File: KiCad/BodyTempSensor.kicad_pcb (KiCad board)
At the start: 2 copper layers, 62 parts, among them IC1 MAX30208CLB+T, J1 USB_C_Receptacle_USB2.0, J2 BAT, J3 TC2030, U1 nRF52840, U2 USBLC6-2SC6, U3 MCP73833-xxx-UN, U4 TLV62568DBVR, U5 MCP6001-OT, Y1 32MHz

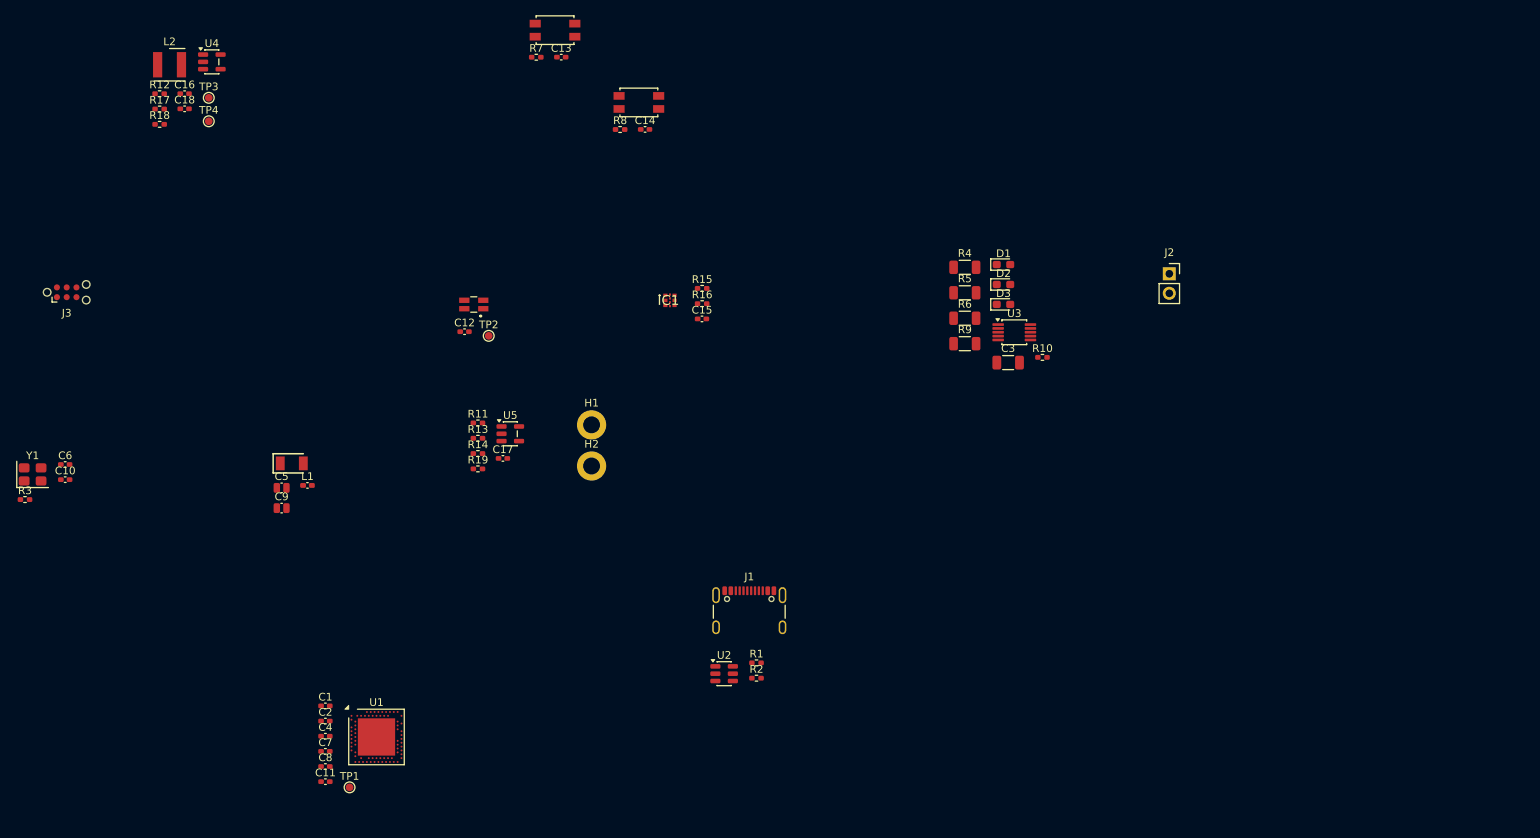
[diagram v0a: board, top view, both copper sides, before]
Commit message: Changed temp sensor, added components and created a general layout design
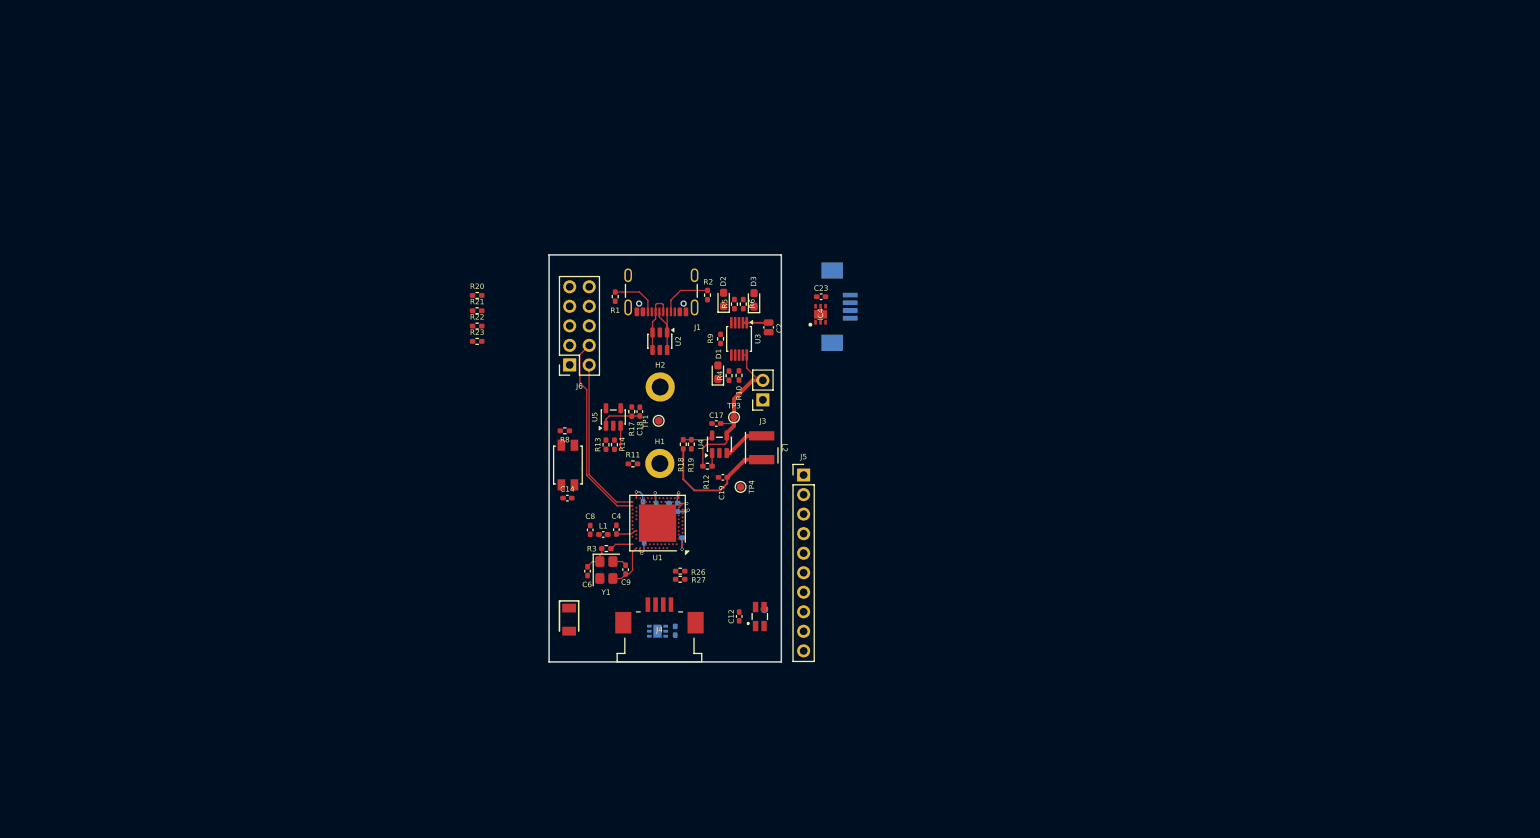
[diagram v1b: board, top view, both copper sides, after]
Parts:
- removed C13, C15: 100n, Capacitor_SMD:C_0402_1005Metric_Pad0.74x0.62mm_HandSolder
- removed C16: 4u7, Capacitor_SMD:C_0402_1005Metric_Pad0.74x0.62mm_HandSolder
- removed IC1: MAX30208CLB+T, PCB_Lib_ItsNotDaan:MAX30208CLBT
- removed J2: BAT, Connector_PinSocket_2.54mm:PinSocket_1x02_P2.54mm_Vertical
- removed R15, R16: 5k1, Resistor_SMD:R_0402_1005Metric_Pad0.72x0.64mm_HandSolder
- removed R7: 10k, Resistor_SMD:R_0402_1005Metric_Pad0.72x0.64mm_HandSolder
- removed RST1: SW_RST, PCB_Lib_ItsNotDaan:SW_SPST_EVQP2
- added C19: 10u, Capacitor_SMD:C_0402_1005Metric_Pad0.74x0.62mm_HandSolder, F.Cu at (120.8, 86.6)
- added C22: 100n, Capacitor_SMD:C_0402_1005Metric_Pad0.74x0.62mm_HandSolder, B.Cu at (114.7, 106.5)
- added C23: 100n, Capacitor_SMD:C_0402_1005Metric_Pad0.74x0.62mm_HandSolder, F.Cu at (133.6, 63.1)
- added IC3: TMP117MAIDRVT, LibLoader:SON65P200X200X80-7N, B.Cu at (112.3, 106.6)
- added IC4: TMP117MAIDRVT, LibLoader:SON65P200X200X80-7N, F.Cu at (133.6, 65.4)
- added J4: 52271-0479, LibLoader:522710479, F.Cu at (112.6, 106.9)
- added J5: Conn_01x10, Connector_PinHeader_2.54mm:PinHeader_1x10_P2.54mm_Vertical, F.Cu at (131.3, 86.3)
- added J6: Conn_02x05_Odd_Even, Connector_PinSocket_2.54mm:PinSocket_2x05_P2.54mm_Vertical, F.Cu at (100.9, 72.0)
- added J7: 52271-0479, LibLoader:522710479, B.Cu at (133.7, 64.4)
- added R20: 10k, Resistor_SMD:R_0402_1005Metric_Pad0.72x0.64mm_HandSolder, F.Cu at (88.9, 63.0)
- added R21: 180k, Resistor_SMD:R_0402_1005Metric_Pad0.72x0.64mm_HandSolder, F.Cu at (88.9, 64.9)
- added R22: 47k, Resistor_SMD:R_0402_1005Metric_Pad0.72x0.64mm_HandSolder, F.Cu at (88.9, 66.9)
- added R23: 180k, Resistor_SMD:R_0402_1005Metric_Pad0.72x0.64mm_HandSolder, F.Cu at (88.9, 68.9)
- added R26: 5k1, Resistor_SMD:R_0402_1005Metric_Pad0.72x0.64mm_HandSolder, F.Cu at (115.3, 98.8)
- added R27: 5k1, Resistor_SMD:R_0402_1005Metric_Pad0.72x0.64mm_HandSolder, F.Cu at (115.3, 99.8)
- C1, C11, C7, TP2: moved to B.Cu
- C10: value 12p -> 100n; moved to B.Cu
- C17: value 270n -> 4u7
- C18: value 10u -> 270n
- C2: value 100n -> 1u; footprint Capacitor_SMD:C_0402_1005Metric_Pad0.74x0.62mm_HandSolder -> Capacitor_SMD:C_0504_1310Metric_Pad0.83x1.28mm_HandSolder
- C3: value 1u -> 100n; footprint Capacitor_SMD:C_1206_3216Metric -> Capacitor_SMD:C_0402_1005Metric_Pad0.74x0.62mm_HandSolder; moved to B.Cu
- C4: value 100n -> 0p8
- C5: value 0p8 -> 100n; footprint Capacitor_SMD:C_0504_1310Metric_Pad0.83x1.28mm_HandSolder -> Capacitor_SMD:C_0402_1005Metric_Pad0.74x0.62mm_HandSolder; moved to B.Cu
- C8: value 100n -> 0p5
- C9: value 0p5 -> 12p; footprint Capacitor_SMD:C_0504_1310Metric_Pad0.83x1.28mm_HandSolder -> Capacitor_SMD:C_0402_1005Metric_Pad0.74x0.62mm_HandSolder
- J3: value TC2030 -> BAT; footprint Connector:Tag-Connect_TC2030-IDC-NL_2x03_P1.27mm_Vertical -> Connector_PinSocket_2.54mm:PinSocket_1x02_P2.54mm_Vertical
- R17: value 450k -> 120k
- R18: value 100k -> 450k
- R19: value 120k -> 100k
- R4, R5, R6, R9: footprint Resistor_SMD:R_1206_3216Metric -> Resistor_SMD:R_0402_1005Metric_Pad0.72x0.64mm_HandSolder
- moved L2 91.7 mm to (125.9, 82.8), turned to -90 degrees
- moved J3 91.6 mm to (126.0, 76.5), turned to 180 degrees
- moved R12 86.1 mm to (118.8, 85.2)
- moved TP4 83.9 mm to (123.2, 87.8), turned to -90 degrees
- moved U4 82.6 mm to (120.4, 82.3), turned to 90 degrees
- moved C10 80.0 mm to (115.0, 94.5), turned to 180 degrees
- moved TP3 79.9 mm to (122.3, 78.8), turned to -90 degrees
- moved R18 79.8 mm to (115.7, 82.3), turned to 90 degrees
- moved C2 77.1 mm to (126.8, 67.1), turned to 90 degrees
- moved R3 75.9 mm to (105.7, 95.9), turned to 180 degrees
- moved Y1 75.6 mm to (105.7, 98.7), turned to -90 degrees
- moved R17 72.9 mm to (109.0, 78.1), turned to -90 degrees
- moved C18 71.1 mm to (110.0, 78.1), turned to -90 degrees
- moved C6 69.3 mm to (103.2, 98.8), turned to -90 degrees
- moved TP1 62.3 mm to (112.5, 79.2), turned to 180 degrees
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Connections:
- C10 pad 1: /OSC_OUT -> +3V3
- C17 pad 1: Net-(U5--) -> VBAT
- C17 pad 2: /P0.02 -> Earth
- C18 pad 1: +3V3 -> Net-(U5--)
- C18 pad 2: Earth -> /P0.02
- C2 pad 1: +3V3 -> Earth
- C2 pad 2: Earth -> VBUS
- C3 pad 1: Earth -> +3V3
- C3 pad 2: VBUS -> Earth
- C4 pad 1: +3V3 -> /RF
- C5 pad 1: /RF -> +3V3
- C8 pad 1: +3V3 -> /RF2
- C9 pad 1: /RF2 -> /OSC_OUT
- J3 pad 1: +3V3 -> Earth
- J3 pad 2: /nRF_SWD_DIO -> VBAT
- R17 pad 1: +3V3 -> Net-(U5--)
- R17 pad 2: Net-(U4-FB) -> /P0.02
- R18 pad 1: Net-(U4-FB) -> +3V3
- R18 pad 2: Earth -> Net-(U4-FB)
- R19 pad 1: Net-(U5--) -> Net-(U4-FB)
- R19 pad 2: /P0.02 -> Earth
- U1 pad AC11: unconnected-(U1-P0.16-PadAC11) -> /P0.16
- U1 pad AD10: unconnected-(U1-P0.15-PadAD10) -> /P0.15
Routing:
- net +3V3: track 0.00 -> 28.6 mm, vias 0 -> 5
- net /nRF_SWD_CLK: track 0.00 -> 25.3 mm
- net VBAT: track 0.00 -> 23.2 mm
- net /nRF_SWD_DIO: track 0.00 -> 21.4 mm
- net VBUS: track 0.00 -> 8.65 mm, vias 0 -> 2
- net /USB_D+: track 0.00 -> 8.11 mm
- net /USB_D-: track 0.00 -> 8.05 mm
- net /USB_CC1: track 0.00 -> 6.80 mm
- net /USB_CC2: track 0.00 -> 6.18 mm
- net /OSC_OUT: track 0.00 -> 6.17 mm
- net Net-(U4-SW): track 0.00 -> 5.48 mm
- net /P0.02: track 0.00 -> 5.42 mm
- net Net-(U4-FB): track 0.00 -> 3.97 mm
- net Net-(C6-Pad1): track 0.00 -> 3.70 mm
- net Net-(U5-+): track 0.00 -> 3.12 mm
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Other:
- board outline added: 30.2 x 52.9 mm
- copper layers 2 -> 4

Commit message: Add Bill of Materials (BOM) for Body Temperature Sensor project
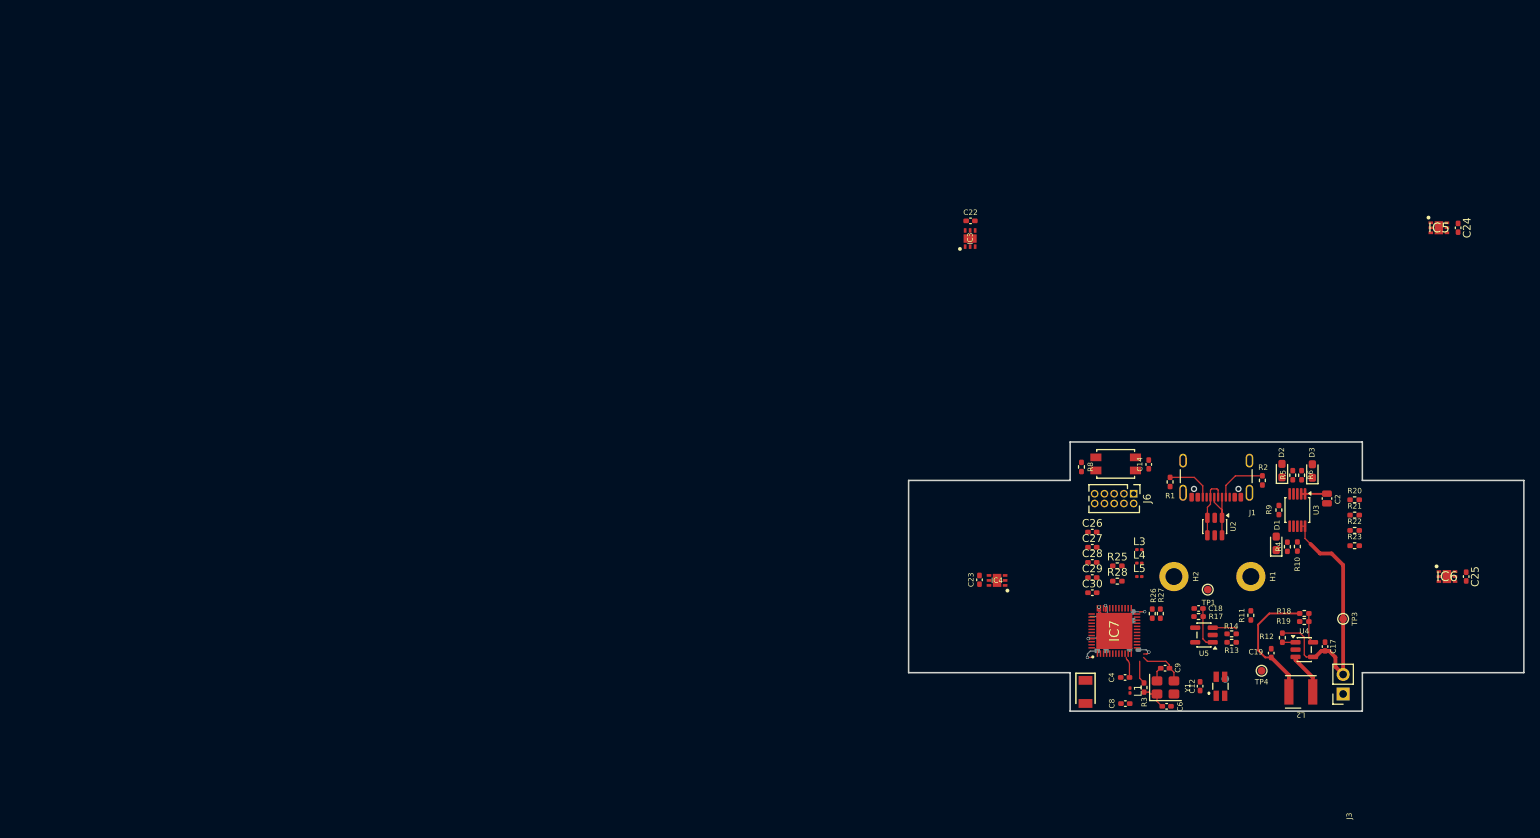
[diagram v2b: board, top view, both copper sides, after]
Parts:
- removed J4, J7: 52271-0479, LibLoader:522710479
- removed J5: Conn_01x10, Connector_PinHeader_2.54mm:PinHeader_1x10_P2.54mm_Vertical
- removed U1: nRF52840, Package_DFN_QFN:Nordic_AQFN-73-1EP_7x7mm_P0.5mm
- added C24: 100n, Capacitor_SMD:C_0402_1005Metric_Pad0.74x0.62mm_HandSolder, F.Cu at (216.4, 54.1)
- added C25: 100n, Capacitor_SMD:C_0402_1005Metric_Pad0.74x0.62mm_HandSolder, F.Cu at (217.5, 99.5)
- added C26: 100n, Capacitor_SMD:C_0402_1005Metric_Pad0.74x0.62mm_HandSolder, F.Cu at (168.9, 93.7)
- added C27: 10n, Capacitor_SMD:C_0402_1005Metric_Pad0.74x0.62mm_HandSolder, F.Cu at (168.9, 95.7)
- added C28: 2u2, Capacitor_SMD:C_0402_1005Metric_Pad0.74x0.62mm_HandSolder, F.Cu at (168.9, 97.7)
- added C29: 2n2, Capacitor_SMD:C_0402_1005Metric_Pad0.74x0.62mm_HandSolder, F.Cu at (168.9, 99.6)
- added C30: 2u2, Capacitor_SMD:C_0402_1005Metric_Pad0.74x0.62mm_HandSolder, F.Cu at (168.9, 101.6)
- added IC5: TMP117MAIDRVT, LibLoader:SON65P200X200X80-7N, F.Cu at (213.9, 54.1)
- added IC6: TMP117MAIDRVT, LibLoader:SON65P200X200X80-7N, F.Cu at (215.0, 99.5)
- added IC7: NRF54L15-QFAA-R, LibLoader:QFN40P600X600X95-49N, F.Cu at (171.8, 106.6)
- added L3: 2.7nH, Inductor_SMD:L_0201_0603Metric, F.Cu at (175.0, 96.0)
- added L4: 3.5nH, Inductor_SMD:L_0201_0603Metric, F.Cu at (175.0, 97.8)
- added L5: 4u7, Inductor_SMD:L_0201_0603Metric, F.Cu at (175.0, 99.5)
- added R25: 10k, Resistor_SMD:R_0402_1005Metric_Pad0.72x0.64mm_HandSolder, F.Cu at (172.1, 98.1)
- added R28: 180k, Resistor_SMD:R_0402_1005Metric_Pad0.72x0.64mm_HandSolder, F.Cu at (172.1, 100.1)
- C18: value 270n -> 390n
- C22: moved to F.Cu
- C4: value 0p8 -> 1p5
- C8: value 0p5 -> 2p
- IC3: value TMP117MAIDRVT -> TMP117MAIDRVR; moved to F.Cu
- J6: footprint Connector_PinSocket_2.54mm:PinSocket_2x05_P2.54mm_Vertical -> Connector_PinHeader_1.27mm:PinHeader_2x05_P1.27mm_Vertical
- L1: value 4n7 -> 3.5nH; footprint Inductor_SMD:L_0402_1005Metric_Pad0.77x0.64mm_HandSolder -> Inductor_SMD:L_0201_0603Metric
- R11: value 330k -> 68k
- R17: value 120k -> 82k
- moved R20 117.2 mm to (203.0, 89.5)
- moved R21 117.2 mm to (203.0, 91.5)
- moved R22 117.2 mm to (203.0, 93.5)
- moved R23 117.2 mm to (203.0, 95.5)
- moved R13 85.3 mm to (187.0, 108.0), turned to 0 degrees
- moved J3 84.6 mm to (201.5, 114.8)
- moved C17 84.3 mm to (199.2, 108.6), turned to 90 degrees
- moved R14 83.9 mm to (187.0, 107.0), turned to 180 degrees
- moved R18 83.7 mm to (196.4, 104.3), turned to 0 degrees
- moved TP3 83.4 mm to (201.5, 105.0), turned to 180 degrees
- moved R19 83.0 mm to (196.4, 105.3), turned to 180 degrees
- moved R11 82.7 mm to (189.5, 104.5), turned to 90 degrees
- moved U5 81.9 mm to (183.4, 107.1), turned to 180 degrees
- moved U4 80.6 mm to (196.4, 109.0), turned to 0 degrees
- moved R17 78.4 mm to (182.7, 104.7), turned to 0 degrees
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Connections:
- net /P0.02 renamed /IO_IMP_OUT
- net /P0.13 renamed /IO_RGB
- net /P0.14 renamed /IO_BTN_ACT
- net /P0.15 renamed /IO_BAT_MEAS
- net /RF renamed Net-(C4-Pad1)
- C8 pad 1: /RF2 -> Net-(C8-Pad1)
- J6 pad 10: unconnected-(J6-Pin_10-Pad10) -> /nRF_RESET
- L1 pad 2: /RF2 -> Net-(C8-Pad1)
- R11 pad 1: /P0.03 -> /IO_IMP_IN
- R20 pad 1: /P0.16 -> /IO_BAT_MEAS_ON
- U5 pad 2: Earth -> /AMP_1
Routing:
- net /nRF_SWD_CLK: track 25.3 -> 0.00 mm
- net /nRF_SWD_DIO: track 21.4 -> 0.00 mm
- net VBAT: track 23.2 -> 35.6 mm
- net VBUS: track 8.65 -> 7.64 mm, vias 2 -> 1
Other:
- board size 30.2 x 52.9 mm -> 80 x 35 mm
